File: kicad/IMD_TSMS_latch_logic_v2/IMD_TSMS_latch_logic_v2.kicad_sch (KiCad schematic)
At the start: 45 parts, among them J1 Conn_01x02, J2 Conn_01x02, J3 Conn_01x02, J4 Conn_01x02, J5 Conn_01x02, J6 Conn_01x02, K1 SANYOU_SRD_Form_C, K2 SANYOU_SRD_Form_C, Q3 AO3400A, Q7 AO3400A, Q8 AO3400A, SW1 SW_Push, U1 4001, U2 4001

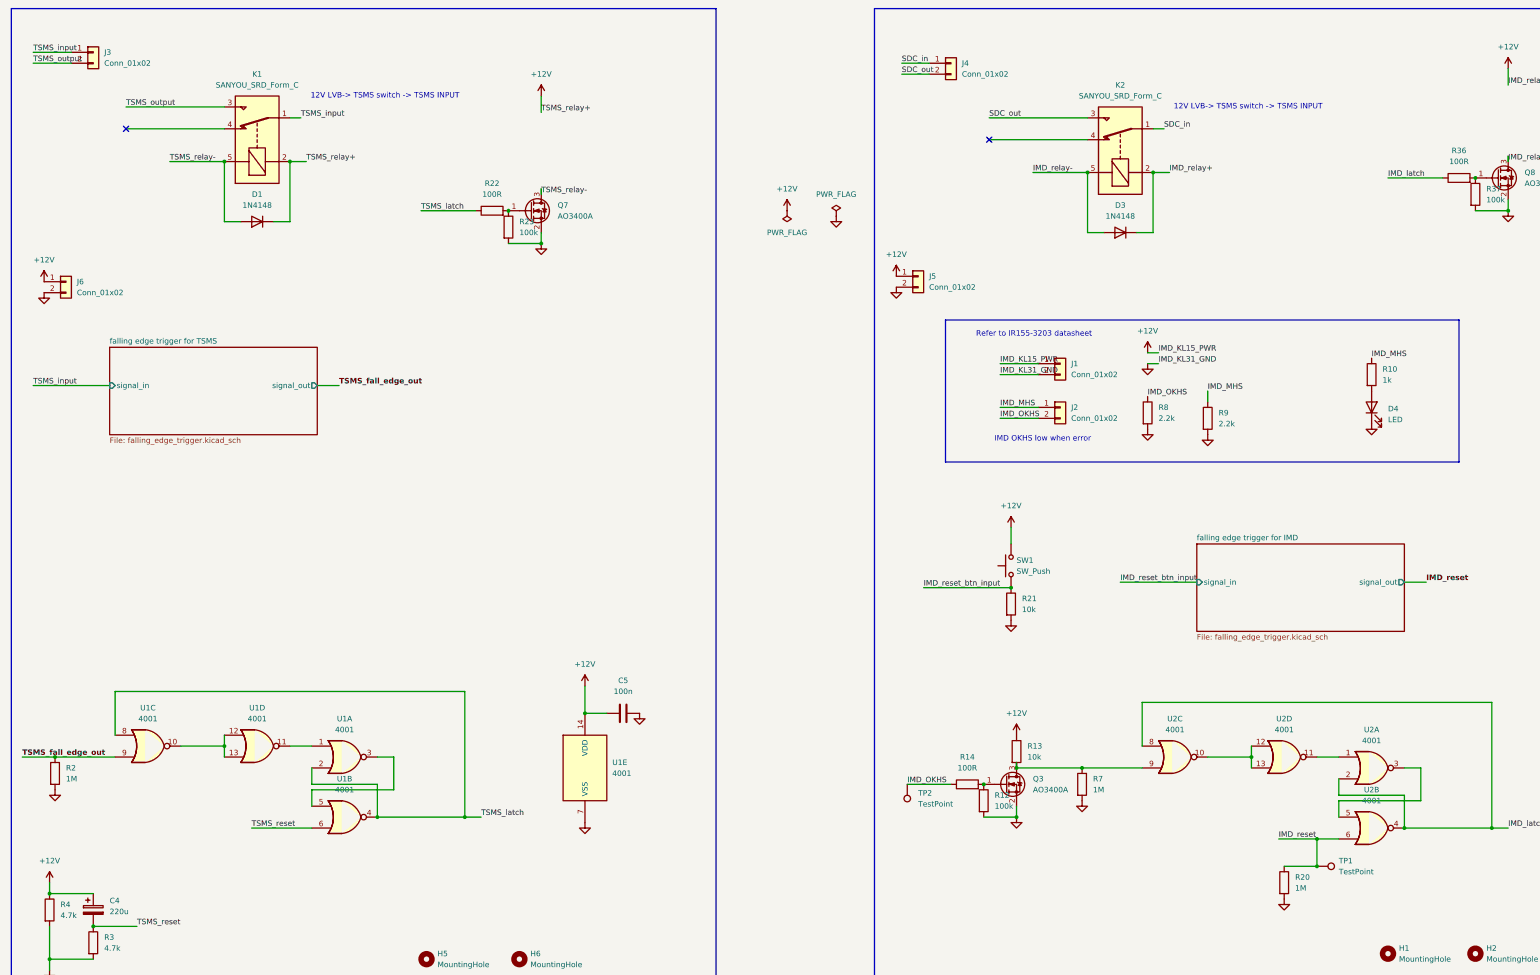
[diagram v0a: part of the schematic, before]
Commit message: minor update on IMD and TSMS latch
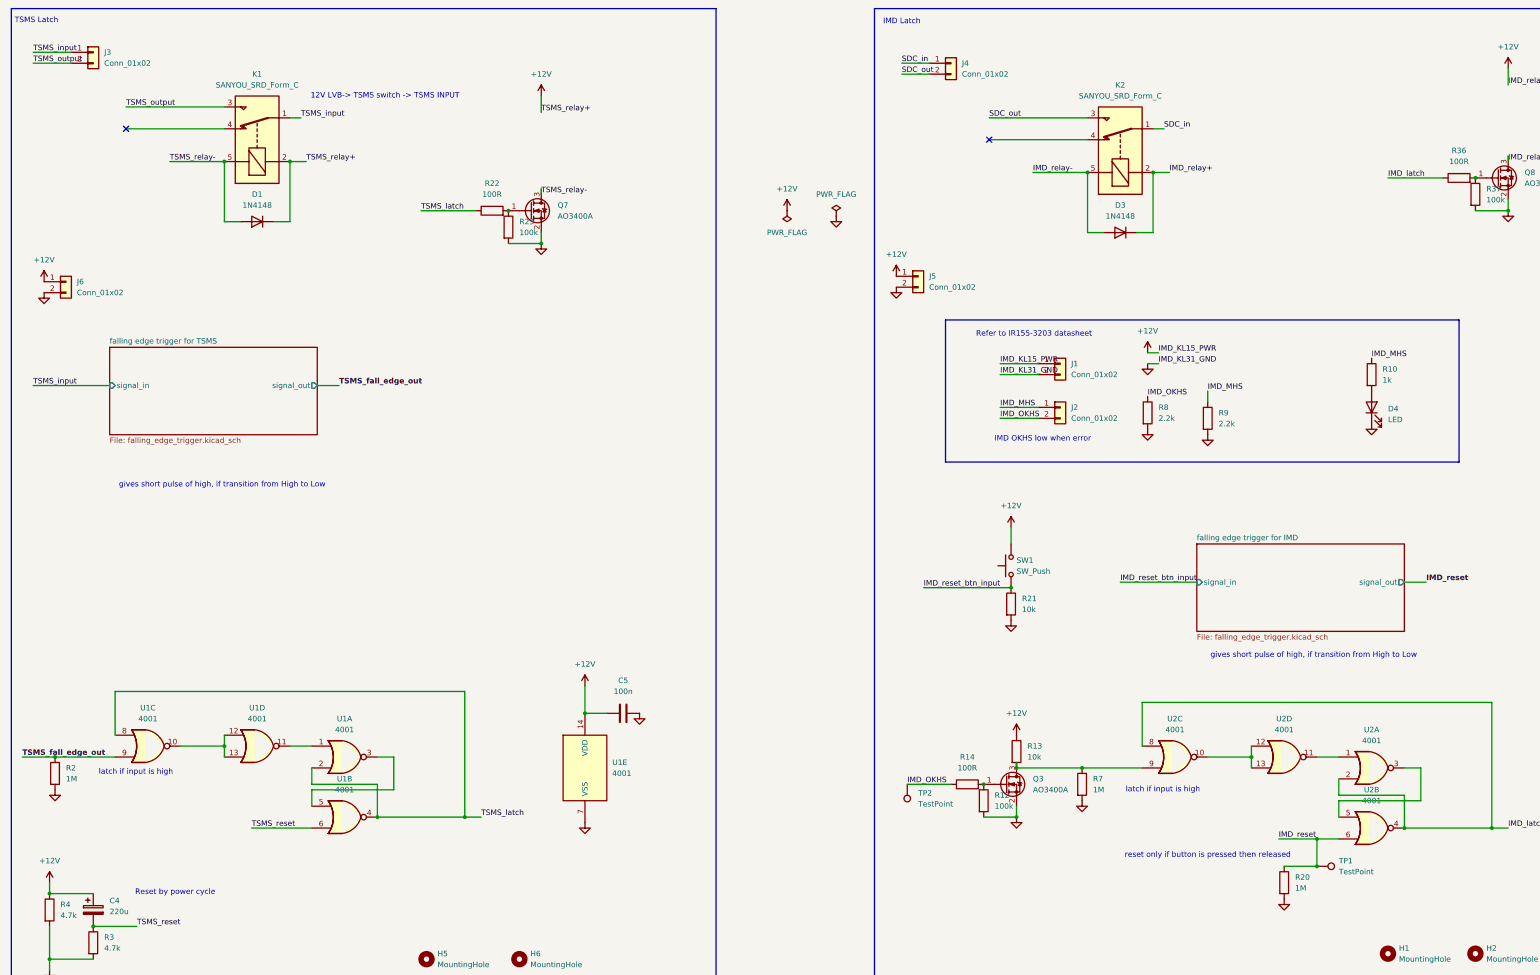
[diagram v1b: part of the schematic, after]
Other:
- note added: "IMD Latch"
- note added: "Reset by power cycle"
- note added: "TSMS Latch"
- note added: "gives short pulse of high, if transition from High to Low"
- note added: "latch if input is high"
- note added: "reset only if button is pressed then released"
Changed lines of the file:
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@@
 		)
 	)
-	(text "12V LVB-> TSMS switch -> TSMS INPUT"
+	(text "reset only if button is pressed then released"
 		(exclude_from_sim no)
-		(at 304.038 40.64 0)
+		(at 294.64 214.63 0)
+		(effects
+			(font
+				(size 1.27 1.27)
+			)
+		)
+	)
+	(text "gives short pulse of high, if transition from High to Low"
+		(exclude_from_sim no)
+		(at 65.532 128.524 0)
+		(effects
+			(font
+				(size 1.27 1.27)
+			)
+		)
+	)
+	(text "gives short pulse of high, if transition from High to Low"
+		(exclude_from_sim no)
+		(at 319.278 168.148 0)
+		(effects
+			(font
+				(size 1.27 1.27)
+			)
+		)
+	)
+	(text "latch if input is high"
+		(exclude_from_sim no)
+		(at 45.466 195.326 0)
+		(effects
+			(font
+				(size 1.27 1.27)
+			)
+		)
+	)
+	(text "latch if input is high"
+		(exclude_from_sim no)
+		(at 284.226 199.39 0)
 		(effects
 			(font
@@
 		(effects
 			(font
+				(size 1.27 1.27)
+			)
+		)
+	)
+	(text "TSMS Latch"
+		(exclude_from_sim no)
+		(at 22.352 20.574 0)
+		(effects
+			(font
+				(size 1.27 1.27)
+			)
+		)
+	)
+	(text "IMD Latch"
+		(exclude_from_sim no)
+		(at 223.52 20.828 0)
+		(effects
+			(font
+				(size 1.27 1.27)
+			)
+		)
+	)
+	(text "Reset by power cycle"
+		(exclude_from_sim no)
+		(at 54.61 223.266 0)
+		(effects
+			(font

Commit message: changed to PMOS to drive relay
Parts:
- removed Q7, Q8: AO3400A, Package_TO_SOT_SMD:SOT-23, symbol Transistor_FET:AO3400A
- added Q4, Q7: AO3401A, Package_TO_SOT_SMD:SOT-23, symbol Transistor_FET:AO3401A
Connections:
- net IMD_relay- is gone; now on net GND: D3.2 (A), K2.5
- net +12V: now also R23.2, R37.2, Q4.2 (S), Q7.2 (S); no longer D1.1 (K), D3.1 (K), K1.2, K2.2
- net GND: now also D1.2 (A), K1.2; no longer R23.2, R37.2
- net SDC_in: now also J4.2 (Pin_2); no longer J4.1 (Pin_1)
- net SDC_out: now also J4.1 (Pin_1), K2.4; no longer J4.2 (Pin_2), K2.3
- net TSMS_input: now also J3.2 (Pin_2); no longer J3.1 (Pin_1)
- net TSMS_output: now also J3.1 (Pin_1), K1.4; no longer J3.2 (Pin_2), K1.3
- net at R36.2, R37.1: now also Q7.1 (G)
- net at R22.2, R23.1: now also Q4.1 (G)
- net TSMS_relay- renamed TSMS_relay+
- net TSMS_relay+: now also D1.1 (K), Q4.3 (D); no longer D1.2 (A)
- new net IMD_relay+: D3.1 (K), K2.2, Q7.3 (D)
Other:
- moved on the sheet: D1

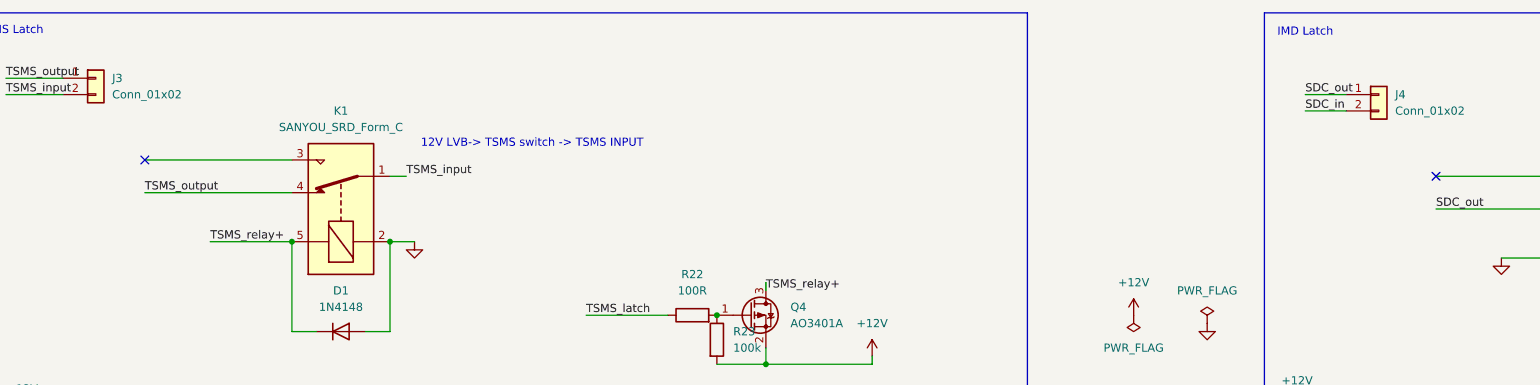
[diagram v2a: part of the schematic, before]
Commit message: added NO NC to avoid confusion
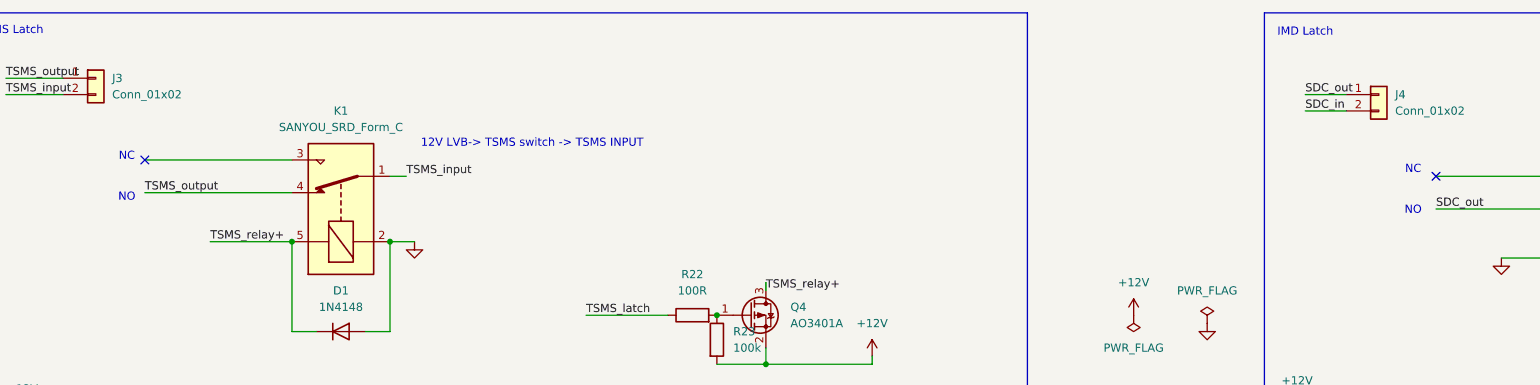
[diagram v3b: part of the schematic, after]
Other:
- note added: "NC"
- note added: "NO"
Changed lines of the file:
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@@
+		)
+	)
+	(text "NC"
+		(exclude_from_sim no)
+		(at 240.284 42.164 0)
+		(effects
+			(font
+				(size 1.27 1.27)
+			)
+		)
+	)
+	(text "NC"
+		(exclude_from_sim no)
+		(at 40.386 40.132 0)
+		(effects
+			(font
+				(size 1.27 1.27)
+			)
 		)
 	)
@@
 		(effects
 			(font
+				(size 1.27 1.27)
+			)
+		)
+	)
+	(text "NO"
+		(exclude_from_sim no)
+		(at 40.386 46.482 0)
+		(effects
+			(font
+				(size 1.27 1.27)
+			)
+		)
+	)
+	(text "NO"
+		(exclude_from_sim no)
+		(at 240.284 48.514 0)
+		(effects
+			(font

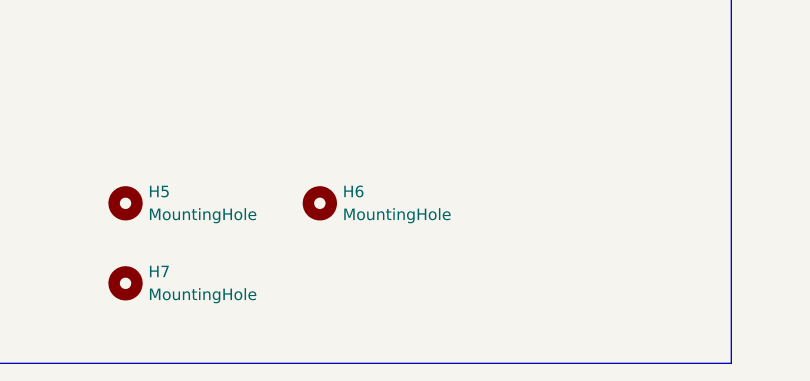
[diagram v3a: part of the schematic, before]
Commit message: added mounting hole, v2 tsms imd latch done
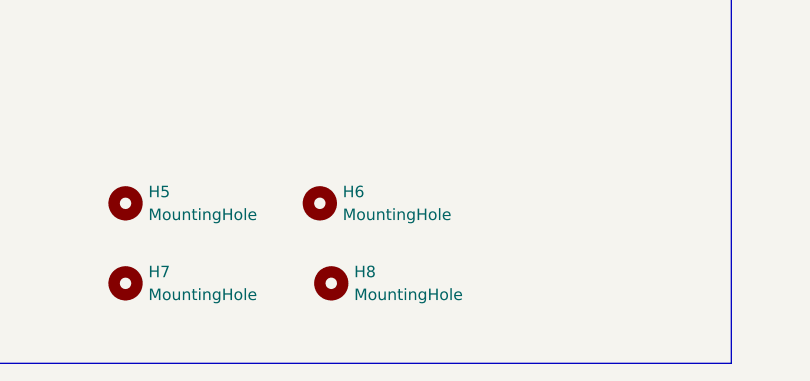
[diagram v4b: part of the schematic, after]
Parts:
- added H8: MountingHole, MountingHole:MountingHole_3.7mm, symbol Mechanical:MountingHole
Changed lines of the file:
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@@
+	)
+	(symbol
+		(lib_id "Mechanical:MountingHole")
+		(at 135.89 247.65 0)
+		(unit 1)
+		(exclude_from_sim no)
+		(in_bom no)
+		(on_board yes)
+		(dnp no)
+		(fields_autoplaced yes)
+		(property "Reference" "H8"
+			(at 138.43 246.3799 0)
+			(effects
+				(font
+					(size 1.27 1.27)
+				)
+				(justify left)
+			)
+		)
+		(property "Value" "MountingHole"
+			(at 138.43 248.9199 0)
+			(effects
+				(font
+					(size 1.27 1.27)
+				)
+				(justify left)
+			)
+		)
+		(property "Footprint" "MountingHole:MountingHole_3.7mm"
+			(at 135.89 247.65 0)
+			(effects
+				(font
+					(size 1.27 1.27)
+				)
+				(hide yes)
+			)
+		)
+		(property "Datasheet" "~"
+			(at 135.89 247.65 0)
+			(effects
+				(font
+					(size 1.27 1.27)
+				)
+				(hide yes)
+			)
+		)
+		(property "Description" "Mounting Hole without connection"
+			(at 135.89 247.65 0)
+			(effects
+				(font
+					(size 1.27 1.27)
+				)
+				(hide yes)
+			)
+		)
+		(instances
+			(project "IMD_TSMS_latch_logic_v2"
+				(path "/84afc6ea-ec4a-4369-9b74-38ac3b8aa9ce"
+					(reference "H8")
+					(unit 1)
+				)
+			)
+		)
 	)
 	(symbol
